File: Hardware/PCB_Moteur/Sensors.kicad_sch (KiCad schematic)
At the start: 18 parts, among them J11 Screw_Terminal_01x04, J18 Screw_Terminal_01x04, U6 MAX6612MXK, U7 INA125UA/2K5

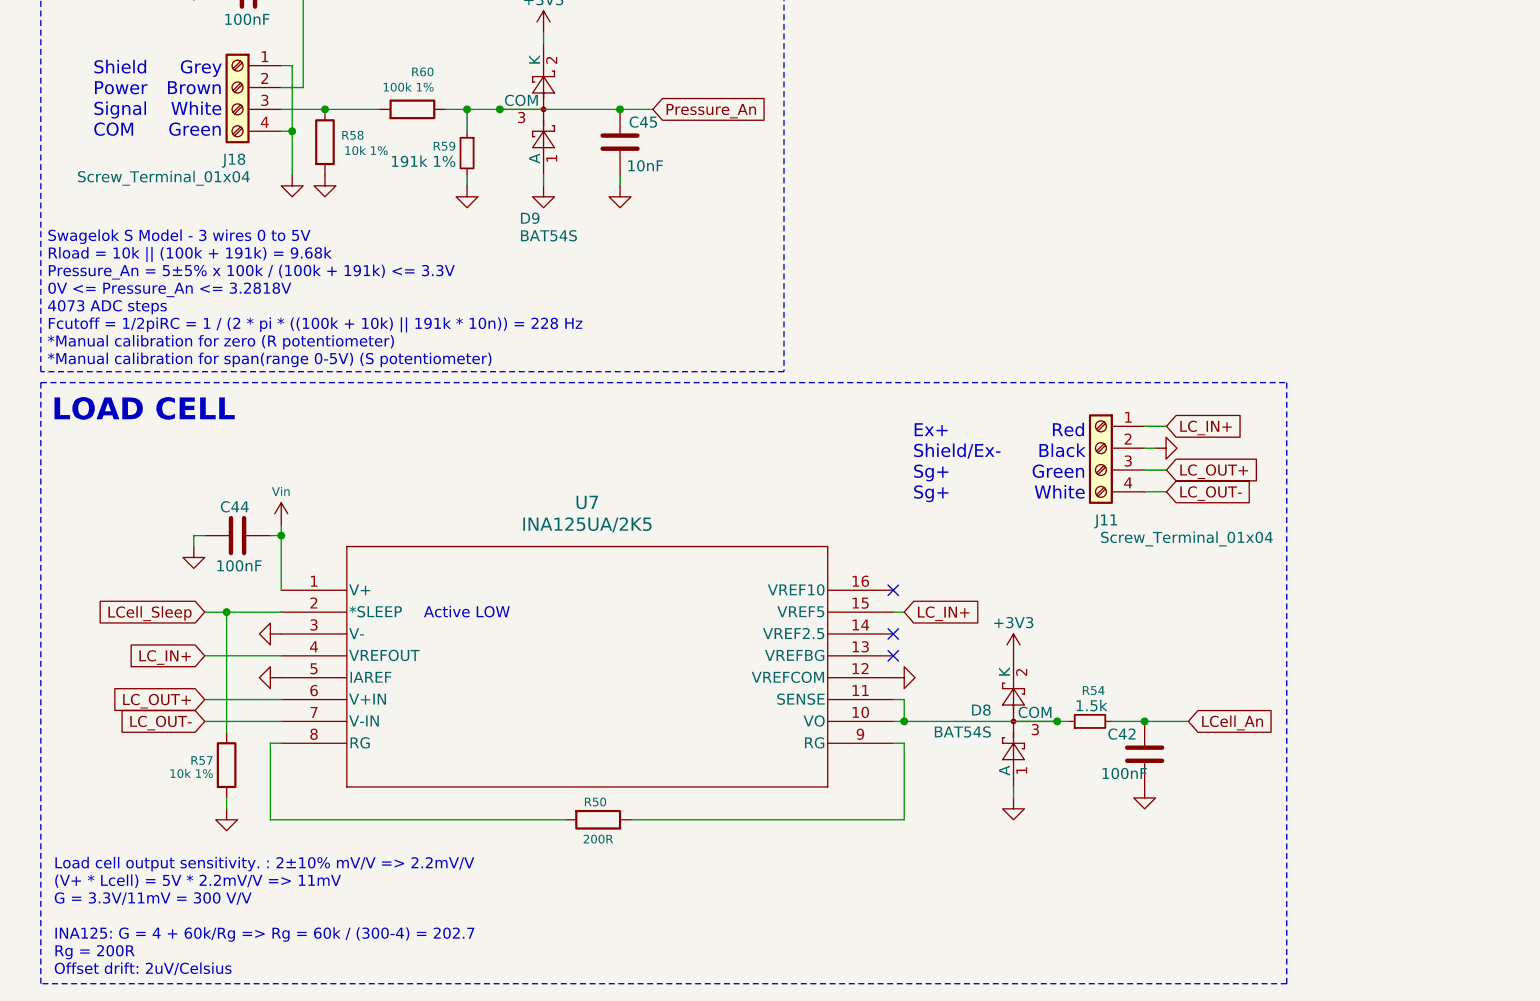
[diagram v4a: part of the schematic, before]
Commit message: fix : BOM errors, change cutoff freq for moteur, minor fixes for GSE
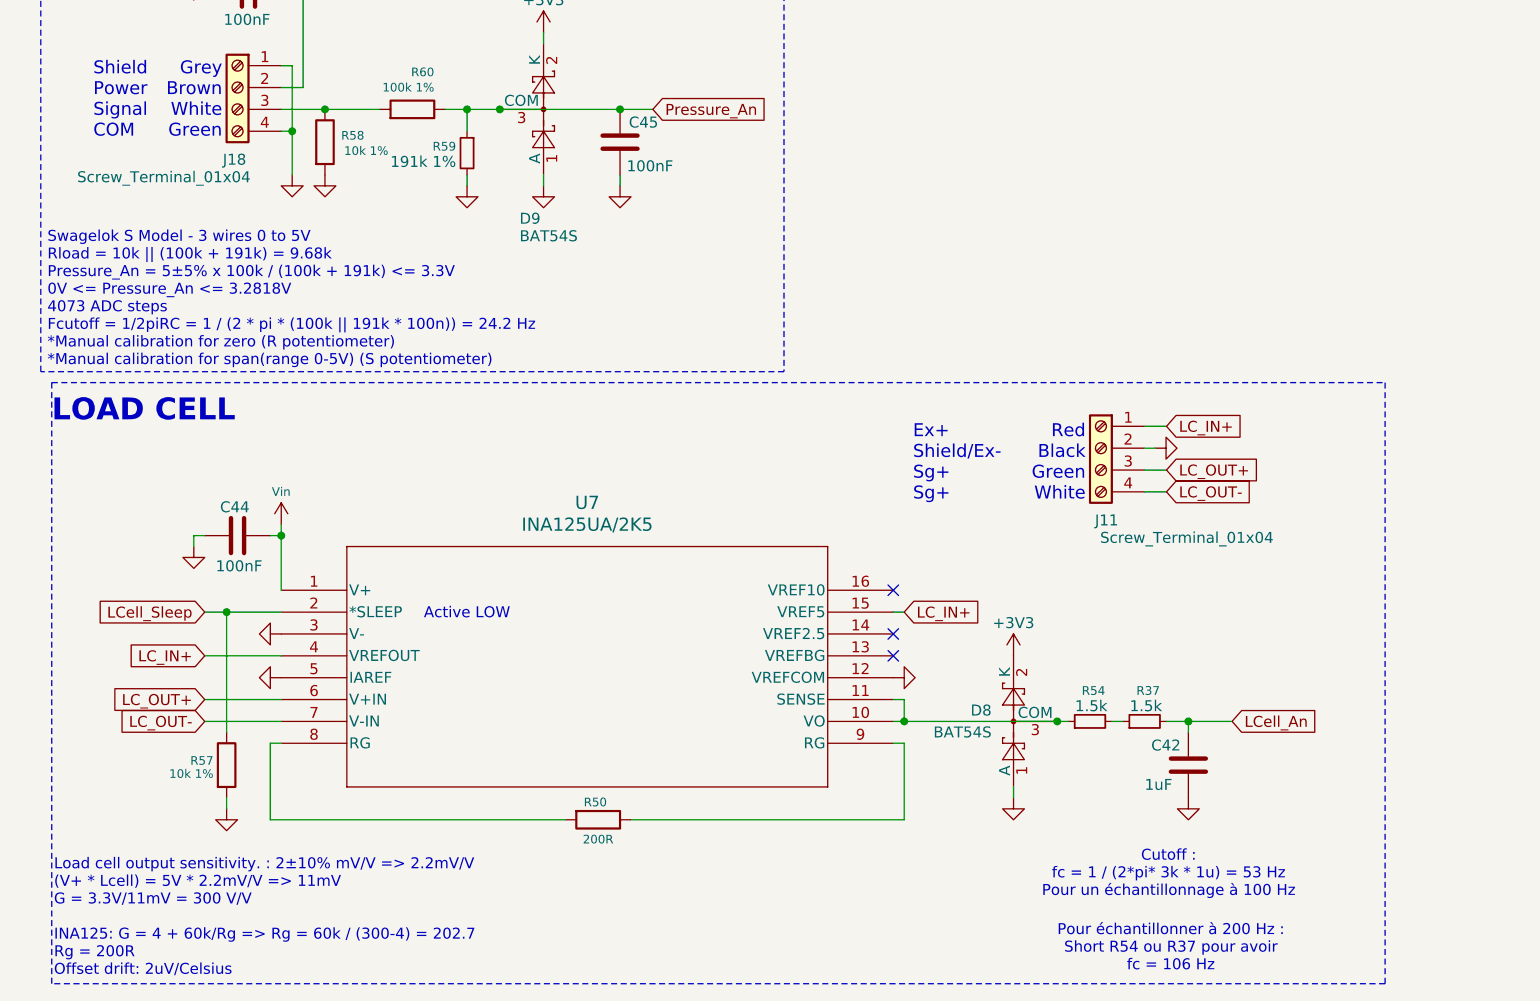
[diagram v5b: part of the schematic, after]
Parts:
- added R37: 1.5k, Resistor_SMD:R_0805_2012Metric, symbol Device:R_Small
- C42: value 100nF -> 1uF; DigiKey_Part_Number 399-C0805C104K5RACTUCT-ND -> 1276-1029-1-ND; Manufacturer_Part_Number C0805C104K5RACTU -> CL21B105KBFNNNE
- C45: value 10nF -> 100nF; footprint Capacitor_SMD:C_0603_1608Metric -> Capacitor_SMD:C_0805_2012Metric; DigiKey_Part_Number 399-C0603C103K5RACTUCT-ND -> 399-C0805C104K5RACTUCT-ND; Manufacturer_Part_Number C0603C103K5RACTU -> C0805C104K5RACTU
- D8, D9: footprint Package_TO_SOT_SMD:SOT-23 -> Package_TO_SOT_SMD:SOT-23-3
- R54: DigiKey_Part_Number P1.5KDBCT-ND -> 311-1.50KCRCT-ND; Manufacturer_Part_Number ERA-3AEB152V -> RC0805FR-071K5L
- R59: DigiKey_Part_Number P191KDBCT-ND -> 311-191KCRCT-ND; Manufacturer_Part_Number ERA-3AEB1913V -> RC0805FR-07191KL
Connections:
- net LCell_An: now also R37.2; no longer R54.2
- new net: R37.1, R54.2
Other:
- note added: "Cutoff : fc = 1 / (2*pi* 3k * 1u) = 53 Hz Pour un échantillonnage à 100 Hz"
- note added: "Pour échantillonner à 200 Hz : Short R54 ou R37 pour avoir fc = 106 Hz"
- note added: "Swagelok S Model - 3 wires 0 to 5V Rload = 10k || (100k + 191k) = 9.68k Pressure_An = 5±5% x 100k / (100k + 191k) <= 3.3V 0V <= Pressure_An <= 3.2818V 4073 ADC steps Fcutoff = 1/2piRC = 1 / (2 * pi * (100k || 191k * 100n)) = 24.2 Hz *Manual calibration for zero (R potentiometer) *Manual calibration for span(range 0-5V) (S potentiometer)"
- note removed: "Swagelok S Model - 3 wires 0 to 5V Rload = 10k || (100k + 191k) = 9.68k Pressure_An = 5±5% x 100k / (100k + 191k) <= 3.3V 0V <= Pressure_An <= 3.2818V 4073 ADC steps Fcutoff = 1/2piRC = 1 / (2 * pi * ((100k + 10k) || 191k * 10n)) = 228 Hz *Manual calibration for zero (R potentiometer) *Manual calibration for span(range 0-5V) (S potentiometer)"
- moved on the sheet: C42

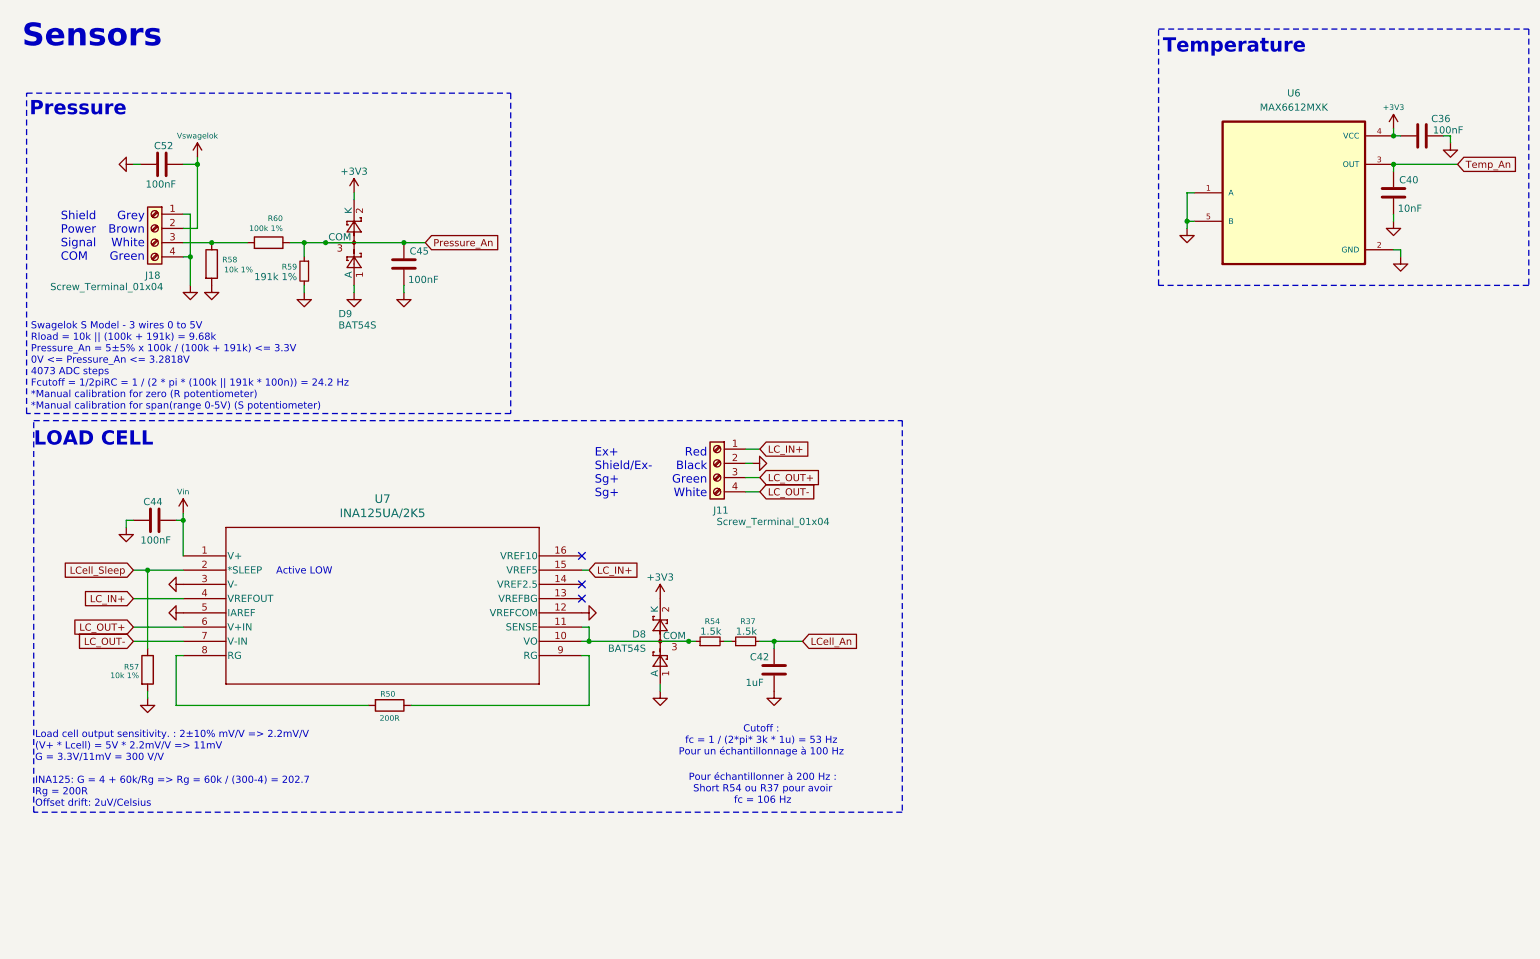
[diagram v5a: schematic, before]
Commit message: fix(moteur): change Swahelok S model -> Swagelok A model (adaptable) + 100R -> 100R 1% + silkscreen
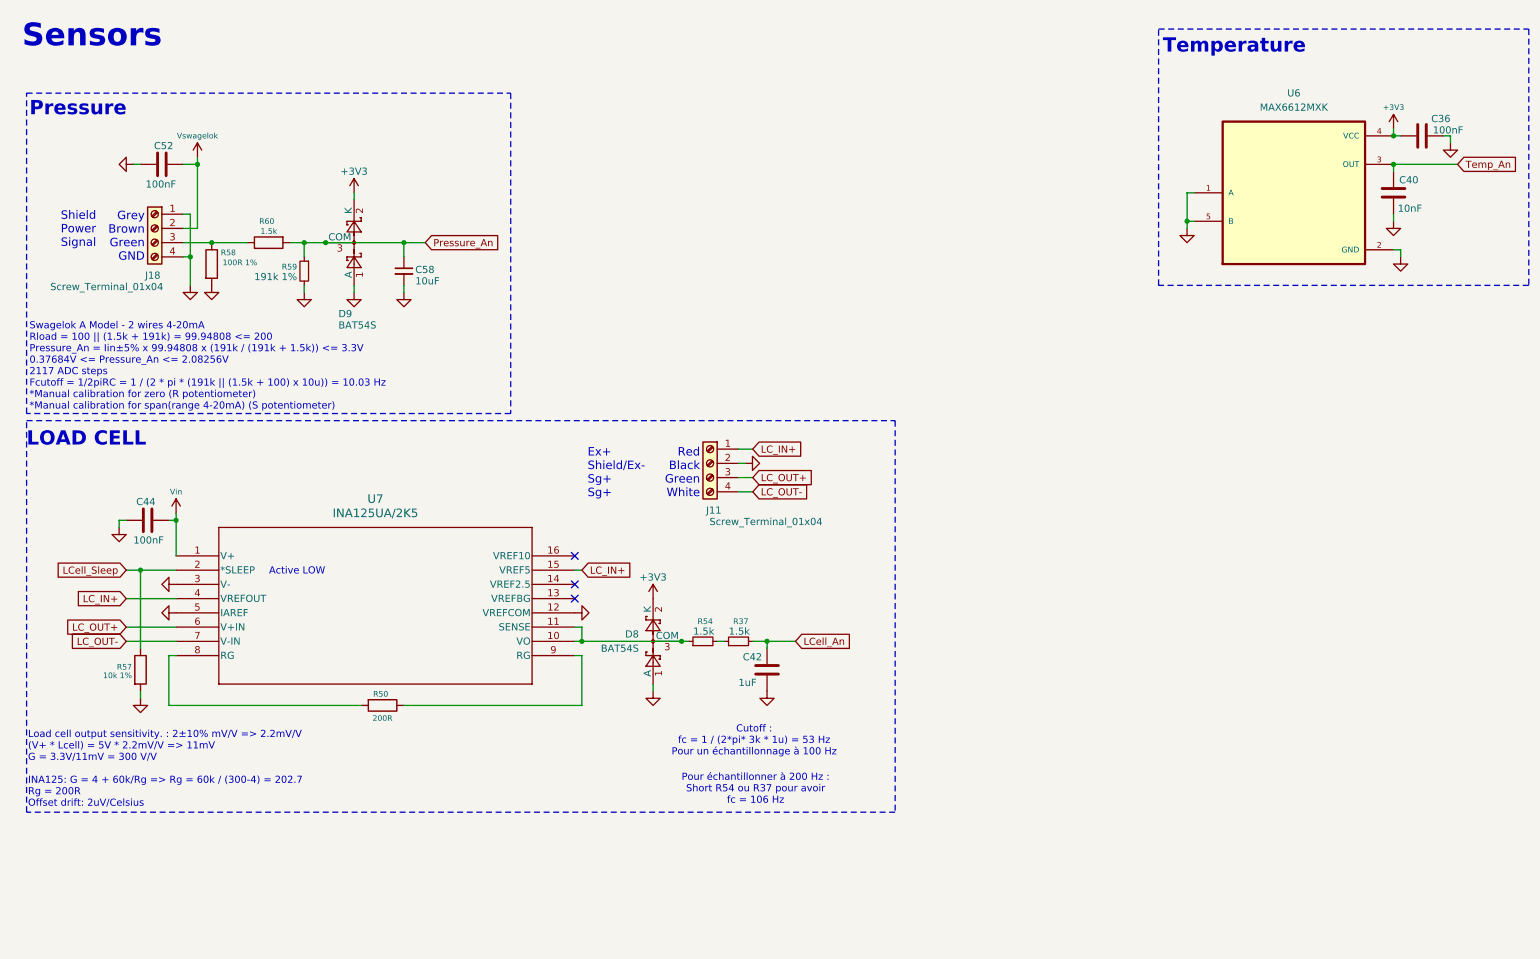
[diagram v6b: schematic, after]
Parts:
- removed C45: 100nF, Capacitor_SMD:C_0805_2012Metric, symbol Device:C
- added C58: 10uF, Capacitor_SMD:C_0805_2012Metric, symbol Device:C_Small
- R58: value 10k 1% -> 100R 1%; DigiKey_Part_Number 541-10.0KCCT-ND -> RT0805FRE07100RL; Manufacturer_Part_Number CRCW080510K0FKEA -> YAG3360CT-ND
- R60: value 100k 1% -> 1.5k; DigiKey_Part_Number 311-100KCRCT-ND -> 311-1.50KCRCT-ND; Manufacturer_Part_Number RC0805FR-07100KL -> RC0805FR-071K5L
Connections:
- net GND: now also C58.2
- net Pressure_An: now also R60.2, C58.1; no longer R60.1
- net at J18.3 (Pin_3), R58.1: now also R60.1; no longer R60.2
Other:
- note added: "Grey Brown Green GND"
- note added: "Shield Power Signal"
- note added: "Swagelok A Model - 2 wires 4-20mA Rload = 100 || (1.5k + 191k) = 99.94808 <= 200 Pressure_An = Iin±5% x 99.94808 x (191k / (191k + 1.5k)) <= 3.3V 0.37684V <= Pressure_An <= 2.08256V 2117 ADC steps Fcutoff = 1/2piRC = 1 / (2 * pi * (191k || (1.5k + 100) x 10u)) = 10.03 Hz *Manual calibration for zero (R potentiometer) *Manual calibration for span(range 4-20mA) (S potentiometer)"
- note removed: "Grey Brown White Green"
- note removed: "Shield Power Signal COM"
- note removed: "Swagelok S Model - 3 wires 0 to 5V Rload = 10k || (100k + 191k) = 9.68k Pressure_An = 5±5% x 100k / (100k + 191k) <= 3.3V 0V <= Pressure_An <= 3.2818V 4073 ADC steps Fcutoff = 1/2piRC = 1 / (2 * pi * (100k || 191k * 100n)) = 24.2 Hz *Manual calibration for zero (R potentiometer) *Manual calibration for span(range 0-5V) (S potentiometer)"
- moved on the sheet: C42, C44, D8, J11, R37, R50, R54, R57, U7
